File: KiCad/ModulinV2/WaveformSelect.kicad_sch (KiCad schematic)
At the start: 72 parts, among them IC18 NC7SZ74K8X, IC19 SN74AHCT1G00DBVR, IC20 SN74AHCT1G00DBVR, IC21 SN74AHCT1G00DBVR, IC22 SN74AHC1G02DBVR, IC23 SN74AHC1G02DBVR, IC24 SN74HC193DR, IC25 TMUX4052DYYR, IC26 TMUX4051DYYRQ1, IC27 TMUX4051DYYRQ1, J5 TSW-104-07-T-D, J6 TSW-104-07-T-D, J7 TSW-104-07-T-D, J8 TSW-104-07-T-D, U1 SN74AHC1G08DBVR

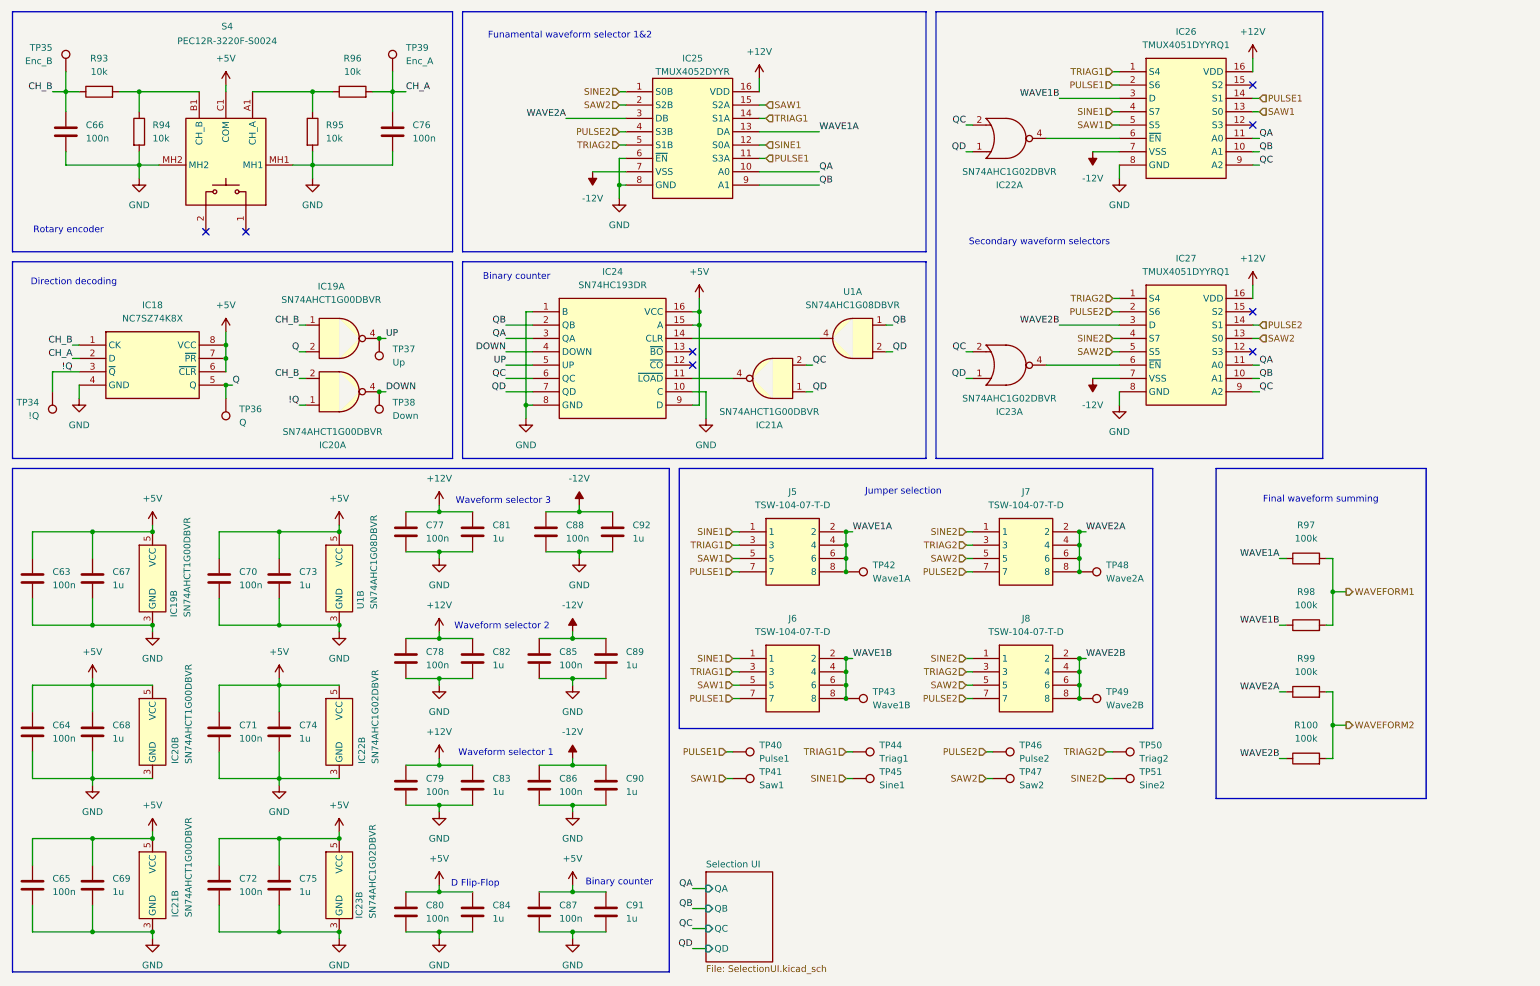
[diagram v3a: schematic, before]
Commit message: Finished Schematic, started on PCB
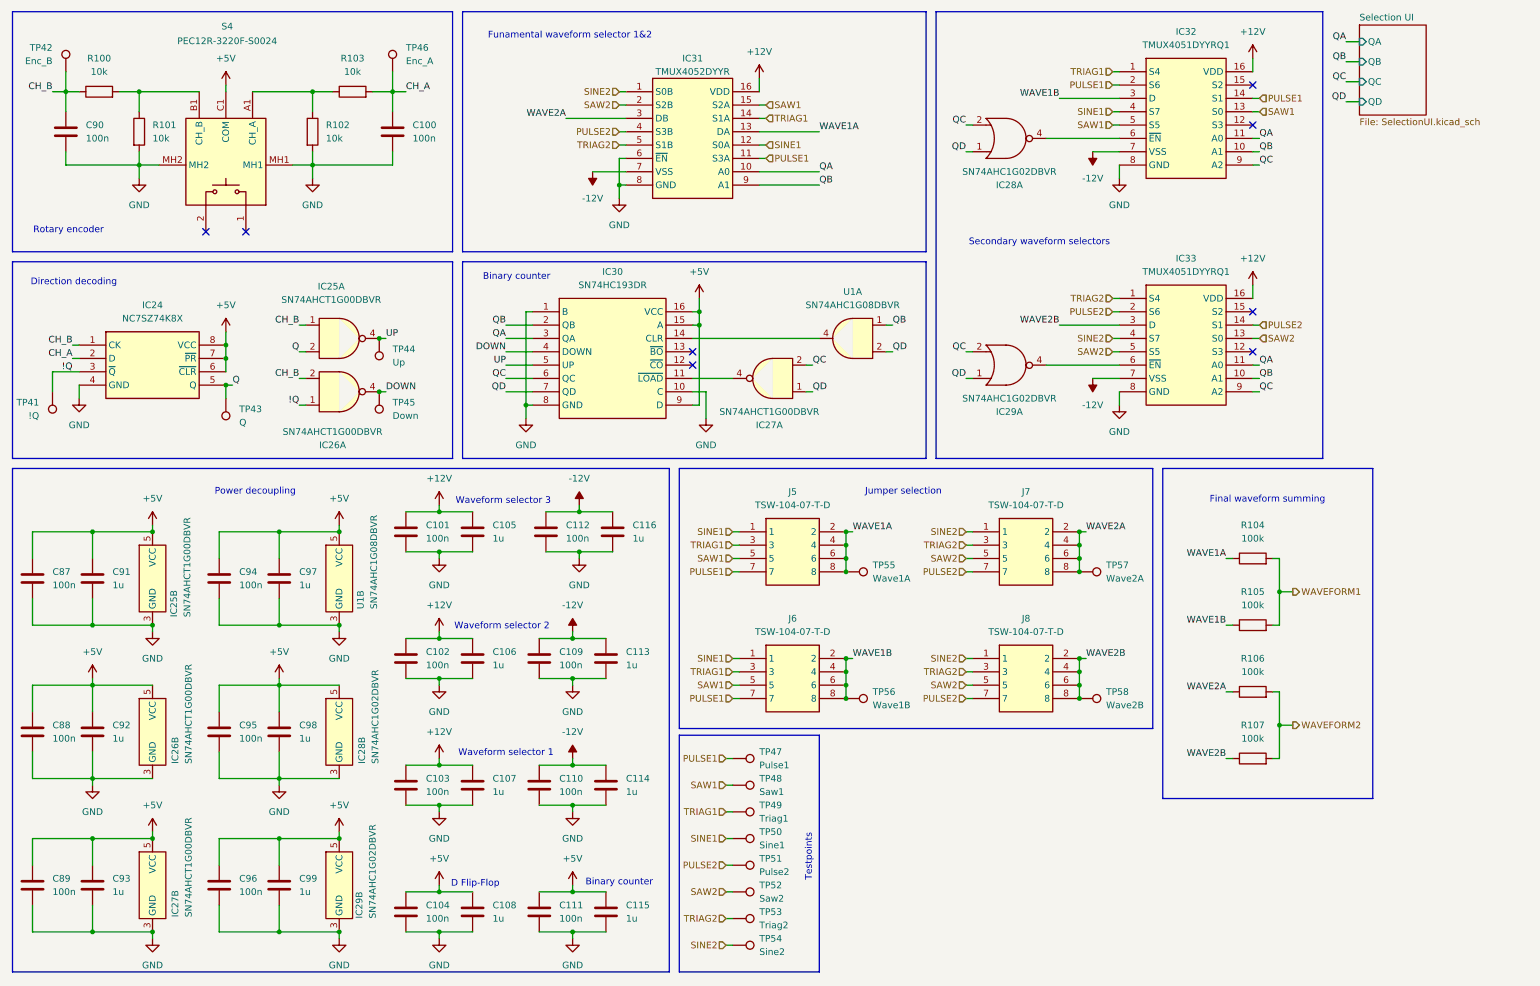
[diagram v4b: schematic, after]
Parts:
- R100: renamed from R93; footprint (none) -> Resistor_SMD:R_0603_1608Metric_Pad0.98x0.95mm_HandSolder
- R101: renamed from R94; footprint (none) -> Resistor_SMD:R_0603_1608Metric_Pad0.98x0.95mm_HandSolder
- R102: renamed from R95; footprint (none) -> Resistor_SMD:R_0603_1608Metric_Pad0.98x0.95mm_HandSolder
- R103: renamed from R96; footprint (none) -> Resistor_SMD:R_0603_1608Metric_Pad0.98x0.95mm_HandSolder
- R104: renamed from R97; footprint (none) -> Resistor_SMD:R_1206_3216Metric_Pad1.30x1.75mm_HandSolder
- R105: renamed from R98; footprint (none) -> Resistor_SMD:R_1206_3216Metric_Pad1.30x1.75mm_HandSolder
- R106: renamed from R99; footprint (none) -> Resistor_SMD:R_1206_3216Metric_Pad1.30x1.75mm_HandSolder
- R107: renamed from R100; footprint (none) -> Resistor_SMD:R_1206_3216Metric_Pad1.30x1.75mm_HandSolder
- renumbered C76 to C100, C77 to C101, C78 to C102, C79 to C103, C80 to C104, C81 to C105, C82 to C106, C83 to C107, C84 to C108, C85 to C109, C86 to C110, C87 to C111, C88 to C112, C89 to C113, C90 to C114, C91 to C115, C92 to C116, C63 to C87, C64 to C88, C65 to C89, C66 to C90, C67 to C91, C68 to C92, C69 to C93, C70 to C94, C71 to C95, C72 to C96, C73 to C97, C74 to C98, C75 to C99, IC18 to IC24, IC19 to IC25, IC20 to IC26, IC21 to IC27, IC22 to IC28, IC23 to IC29, IC24 to IC30, IC25 to IC31, IC26 to IC32, IC27 to IC33, TP34 to TP41, TP35 to TP42, TP36 to TP43, TP37 to TP44, TP38 to TP45, TP39 to TP46, TP40 to TP47, TP41 to TP48, TP44 to TP49, TP45 to TP50, TP46 to TP51, TP47 to TP52, TP50 to TP53, TP51 to TP54, TP42 to TP55, TP43 to TP56, TP48 to TP57, TP49 to TP58
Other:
- note added: "Power decoupling"
- note added: "Testpoints"
- moved on the sheet: R104, R105, R106, R107, TP47, TP48, TP49, TP50, TP51, TP52, TP53, TP54

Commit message: Layed out Interface and PWR components and started with MCU layout
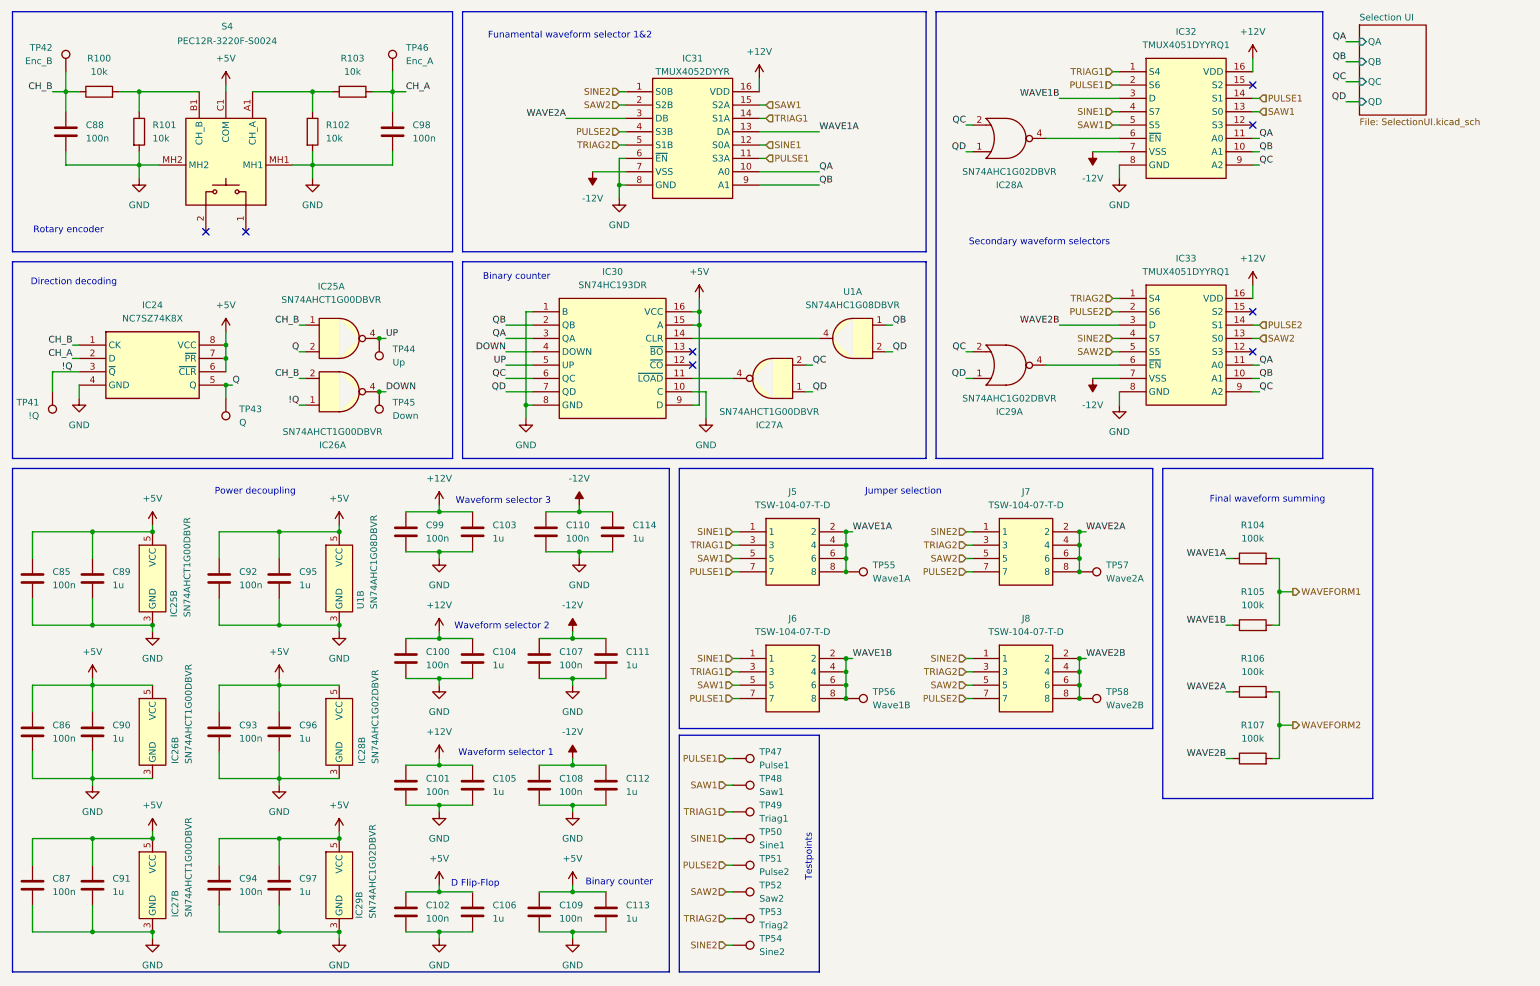
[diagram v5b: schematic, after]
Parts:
- renumbered C102 to C100, C103 to C101, C104 to C102, C105 to C103, C106 to C104, C107 to C105, C108 to C106, C109 to C107, C110 to C108, C111 to C109, C112 to C110, C113 to C111, C114 to C112, C115 to C113, C116 to C114, C87 to C85, C88 to C86, C89 to C87, C90 to C88, C91 to C89, C92 to C90, C93 to C91, C94 to C92, C95 to C93, C96 to C94, C97 to C95, C98 to C96, C99 to C97, C100 to C98, C101 to C99
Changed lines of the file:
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@@
 		(dnp no)
 		(fields_autoplaced yes)
-		(property "Reference" "C108"
+		(property "Reference" "C106"
 			(at 105.41 184.1499 0)
 			(effects
@@
 			(project "ModulinV2"
 				(path "/c6b34a57-3941-4b56-8b80-1848c7f41082/ba5ade70-a939-4914-9429-1ad400c74d73"
-					(reference "C108")
+					(reference "C106")
 					(unit 1)
 				)
@@
 		(dnp no)
 		(fields_autoplaced yes)
-		(property "Reference" "C106"
+		(property "Reference" "C104"
 			(at 105.41 135.8899 0)
 			(effects
@@
 			(project "ModulinV2"
 				(path "/c6b34a57-3941-4b56-8b80-1848c7f41082/ba5ade70-a939-4914-9429-1ad400c74d73"
-					(reference "C106")
+					(reference "C104")
 					(unit 1)
 				)
@@
 		(dnp no)
 		(fields_autoplaced yes)
-		(property "Reference" "C94"
+		(property "Reference" "C92"
 			(at 57.15 120.6499 0)
 			(effects
@@
 			(project "ModulinV2"
 				(path "/c6b34a57-3941-4b56-8b80-1848c7f41082/ba5ade70-a939-4914-9429-1ad400c74d73"
-					(reference "C94")
+					(reference "C92")
 					(unit 1)
 				)
@@
 		(dnp no)
 		(fields_autoplaced yes)
-		(property "Reference" "C90"
+		(property "Reference" "C88"
 			(at 27.94 35.5599 0)
 			(effects
@@
 			(project ""
 				(path "/c6b34a57-3941-4b56-8b80-1848c7f41082/ba5ade70-a939-4914-9429-1ad400c74d73"
-					(reference "C90")
+					(reference "C88")
 					(unit 1)
 				)
@@
 		(dnp no)
 		(fields_autoplaced yes)
-		(property "Reference" "C93"
+		(property "Reference" "C91"
 			(at 33.02 179.0699 0)
 			(effects
@@
 			(project "ModulinV2"
 				(path "/c6b34a57-3941-4b56-8b80-1848c7f41082/ba5ade70-a939-4914-9429-1ad400c74d73"
-					(reference "C93")
+					(reference "C91")
 					(unit 1)
 				)
@@
 		(dnp no)
 		(fields_autoplaced yes)
-		(property "Reference" "C107"
+		(property "Reference" "C105"
 			(at 105.41 160.0199 0)
 			(effects
@@
 			(project "ModulinV2"
 				(path "/c6b34a57-3941-4b56-8b80-1848c7f41082/ba5ade70-a939-4914-9429-1ad400c74d73"
-					(reference "C107")
+					(reference "C105")
 					(unit 1)
 				)
@@
 		(dnp no)
 		(fields_autoplaced yes)
-		(property "Reference" "C89"
+		(property "Reference" "C87"
 			(at 21.59 179.0699 0)
 			(effects
@@
 			(project "ModulinV2"
 				(path "/c6b34a57-3941-4b56-8b80-1848c7f41082/ba5ade70-a939-4914-9429-1ad400c74d73"
-					(reference "C89")
+					(reference "C87")
 					(unit 1)
 				)
@@
 		(dnp no)
 		(fields_autoplaced yes)
-		(property "Reference" "C105"
+		(property "Reference" "C103"
 			(at 105.41 111.7599 0)
 			(effects
@@
 			(project "ModulinV2"
 				(path "/c6b34a57-3941-4b56-8b80-1848c7f41082/ba5ade70-a939-4914-9429-1ad400c74d73"
-					(reference "C105")
+					(reference "C103")
 					(unit 1)
 				)
@@
 		(dnp no)
 		(fields_autoplaced yes)
-		(property "Reference" "C95"
+		(property "Reference" "C93"
 			(at 57.15 149.8599 0)
 			(effects
@@
 			(project "ModulinV2"
 				(path "/c6b34a57-3941-4b56-8b80-1848c7f41082/ba5ade70-a939-4914-9429-1ad400c74d73"
-					(reference "C95")
+					(reference "C93")
 					(unit 1)
 				)
@@
 		(dnp no)
 		(fields_autoplaced yes)
-		(property "Reference" "C114"
+		(property "Reference" "C112"
 			(at 130.81 160.0199 0)
 			(effects
@@
 			(project "ModulinV2"
 				(path "/c6b34a57-3941-4b56-8b80-1848c7f41082/ba5ade70-a939-4914-9429-1ad400c74d73"
-					(reference "C114")
+					(reference "C112")
 					(unit 1)
 				)
@@
 		(dnp no)
 		(fields_autoplaced yes)
-		(property "Reference" "C98"
+		(property "Reference" "C96"
 			(at 68.58 149.8599 0)
 			(effects
@@
 			(project "ModulinV2"
 				(path "/c6b34a57-3941-4b56-8b80-1848c7f41082/ba5ade70-a939-4914-9429-1ad400c74d73"
-					(reference "C98")
+					(reference "C96")
 					(unit 1)
 				)
@@
 		(dnp no)
 		(fields_autoplaced yes)
-		(property "Reference" "C91"
+		(property "Reference" "C89"
 			(at 33.02 120.6499 0)
 			(effects
@@
 			(project "ModulinV2"
 				(path "/c6b34a57-3941-4b56-8b80-1848c7f41082/ba5ade70-a939-4914-9429-1ad400c74d73"
-					(reference "C91")
+					(reference "C89")
 					(unit 1)
 				)
@@
 		(dnp no)
 		(fields_autoplaced yes)
-		(property "Reference" "C112"
+		(property "Reference" "C110"
 			(at 119.38 111.7599 0)
 			(effects
@@
 			(project "ModulinV2"
 				(path "/c6b34a57-3941-4b56-8b80-1848c7f41082/ba5ade70-a939-4914-9429-1ad400c74d73"
-					(reference "C112")
+					(reference "C110")
 					(unit 1)
 				)
@@
 		(dnp no)
 		(fields_autoplaced yes)
-		(property "Reference" "C104"
+		(property "Reference" "C102"
 			(at 92.71 184.1499 0)
 			(effects
@@
 			(project "ModulinV2"
 				(path "/c6b34a57-3941-4b56-8b80-1848c7f41082/ba5ade70-a939-4914-9429-1ad400c74d73"
-					(reference "C104")
+					(reference "C102")
 					(unit 1)
 				)
@@
 		(dnp no)
 		(fields_autoplaced yes)
-		(property "Reference" "C97"
+		(property "Reference" "C95"
 			(at 68.58 120.6499 0)
 			(effects
@@
 			(project "ModulinV2"
 				(path "/c6b34a57-3941-4b56-8b80-1848c7f41082/ba5ade70-a939-4914-9429-1ad400c74d73"
-					(reference "C97")
+					(reference "C95")
 					(unit 1)
 				)
@@
 		(dnp no)
 		(fields_autoplaced yes)
-		(property "Reference" "C102"
+		(property "Reference" "C100"
 			(at 92.71 135.8899 0)
 			(effects
@@
 			(project "ModulinV2"
 				(path "/c6b34a57-3941-4b56-8b80-1848c7f41082/ba5ade70-a939-4914-9429-1ad400c74d73"
-					(reference "C102")
+					(reference "C100")
 					(unit 1)
 				)
@@
 		(dnp no)
 		(fields_autoplaced yes)
-		(property "Reference" "C99"
+		(property "Reference" "C97"
 			(at 68.58 179.0699 0)
 			(effects
@@
 			(project "ModulinV2"
 				(path "/c6b34a57-3941-4b56-8b80-1848c7f41082/ba5ade70-a939-4914-9429-1ad400c74d73"
-					(reference "C99")
+					(reference "C97")
 					(unit 1)
 				)
@@
 		(dnp no)
 		(fields_autoplaced yes)
-		(property "Reference" "C109"
+		(property "Reference" "C107"
 			(at 118.11 135.8899 0)
 			(effects
@@
 			(project "ModulinV2"
 				(path "/c6b34a57-3941-4b56-8b80-1848c7f41082/ba5ade70-a939-4914-9429-1ad400c74d73"
-					(reference "C109")
+					(reference "C107")
 					(unit 1)
 				)
@@
 		(dnp no)
 		(fields_autoplaced yes)
-		(property "Reference" "C88"
+		(property "Reference" "C86"
 			(at 21.59 149.8599 0)
 			(effects
@@
 			(project "ModulinV2"
 				(path "/c6b34a57-3941-4b56-8b80-1848c7f41082/ba5ade70-a939-4914-9429-1ad400c74d73"
-					(reference "C88")
+					(reference "C86")
 					(unit 1)
 				)
@@
 		(dnp no)
 		(fields_autoplaced yes)
-		(property "Reference" "C103"
+		(property "Reference" "C101"
 			(at 92.71 160.0199 0)
 			(effects
@@
 			(project "ModulinV2"
 				(path "/c6b34a57-3941-4b56-8b80-1848c7f41082/ba5ade70-a939-4914-9429-1ad400c74d73"
-					(reference "C103")
+					(reference "C101")
 					(unit 1)
 				)
@@
 		(dnp no)
 		(fields_autoplaced yes)
-		(property "Reference" "C115"
+		(property "Reference" "C113"
 			(at 130.81 184.1499 0)
 			(effects
@@
 			(project "ModulinV2"
 				(path "/c6b34a57-3941-4b56-8b80-1848c7f41082/ba5ade70-a939-4914-9429-1ad400c74d73"
-					(reference "C115")
+					(reference "C113")
 					(unit 1)
 				)
@@
 		(dnp no)
 		(fields_autoplaced yes)
-		(property "Reference" "C87"
+		(property "Reference" "C85"
 			(at 21.59 120.6499 0)
 			(effects
@@
 			(project "ModulinV2"
 				(path "/c6b34a57-3941-4b56-8b80-1848c7f41082/ba5ade70-a939-4914-9429-1ad400c74d73"
-					(reference "C87")
+					(reference "C85")
 					(unit 1)
 				)
@@
 		(dnp no)
 		(fields_autoplaced yes)
-		(property "Reference" "C96"
+		(property "Reference" "C94"
 			(at 57.15 179.0699 0)
 			(effects
@@
 			(project "ModulinV2"
 				(path "/c6b34a57-3941-4b56-8b80-1848c7f41082/ba5ade70-a939-4914-9429-1ad400c74d73"
-					(reference "C96")
+					(reference "C94")
 					(unit 1)
 				)
@@
 		(dnp no)
 		(fields_autoplaced yes)
-		(property "Reference" "C113"
+		(property "Reference" "C111"
 			(at 130.81 135.8899 0)
 			(effects
@@
 			(project "ModulinV2"
 				(path "/c6b34a57-3941-4b56-8b80-1848c7f41082/ba5ade70-a939-4914-9429-1ad400c74d73"
-					(reference "C113")
+					(reference "C111")
 					(unit 1)
 				)
@@
 		(dnp no)
 		(fields_autoplaced yes)
-		(property "Reference" "C92"
+		(property "Reference" "C90"
 			(at 33.02 149.8599 0)
 			(effects
@@
 			(project "ModulinV2"
 				(path "/c6b34a57-3941-4b56-8b80-1848c7f41082/ba5ade70-a939-4914-9429-1ad400c74d73"
-					(reference "C92")
+					(reference "C90")
 					(unit 1)
 				)
@@
 		(dnp no)
 		(fields_autoplaced yes)
-		(property "Reference" "C116"
+		(property "Reference" "C114"
 			(at 132.08 111.7599 0)
 			(effects
@@
 			(project "ModulinV2"
 				(path "/c6b34a57-3941-4b56-8b80-1848c7f41082/ba5ade70-a939-4914-9429-1ad400c74d73"
-					(reference "C116")
+					(reference "C114")
 					(unit 1)
 				)
@@
 		(dnp no)
 		(fields_autoplaced yes)
-		(property "Reference" "C101"
+		(property "Reference" "C99"
 			(at 92.71 111.7599 0)
 			(effects
@@
 			(project "ModulinV2"
 				(path "/c6b34a57-3941-4b56-8b80-1848c7f41082/ba5ade70-a939-4914-9429-1ad400c74d73"
-					(reference "C101")
+					(reference "C99")
 					(unit 1)
 				)
@@
 		(dnp no)
 		(fields_autoplaced yes)
-		(property "Reference" "C100"
+		(property "Reference" "C98"
 			(at 90.17 35.5599 0)
 			(effects
@@
 			(project "ModulinV2"
 				(path "/c6b34a57-3941-4b56-8b80-1848c7f41082/ba5ade70-a939-4914-9429-1ad400c74d73"
-					(reference "C100")
+					(reference "C98")
 					(unit 1)
 				)
@@
 		(dnp no)
 		(fields_autoplaced yes)
-		(property "Reference" "C110"
+		(property "Reference" "C108"
 			(at 118.11 160.0199 0)
 			(effects
@@
 			(project "ModulinV2"
 				(path "/c6b34a57-3941-4b56-8b80-1848c7f41082/ba5ade70-a939-4914-9429-1ad400c74d73"
-					(reference "C110")
+					(reference "C108")
 					(unit 1)
 				)
@@
 		(dnp no)
 		(fields_autoplaced yes)
-		(property "Reference" "C111"
+		(property "Reference" "C109"
 			(at 118.11 184.1499 0)
 			(effects
@@
 			(project "ModulinV2"
 				(path "/c6b34a57-3941-4b56-8b80-1848c7f41082/ba5ade70-a939-4914-9429-1ad400c74d73"
-					(reference "C111")
+					(reference "C109")
 					(unit 1)
 				)
